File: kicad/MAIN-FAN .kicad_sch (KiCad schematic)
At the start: 8 parts, among them J14 MAIN-FAN, Q14 AO3401, Q15 2N3904

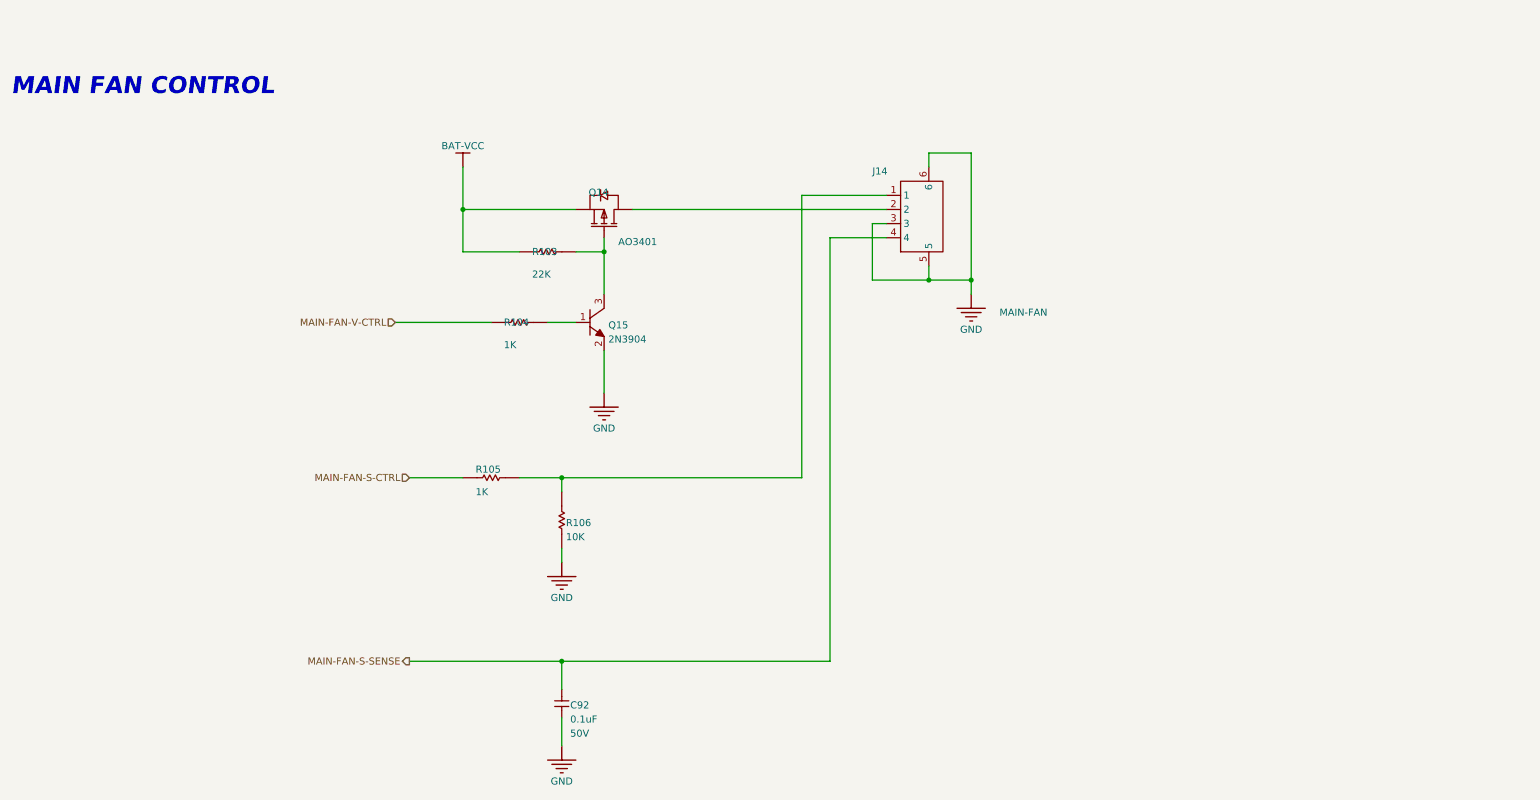
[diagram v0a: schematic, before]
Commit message: Added Pi CM4/CM5
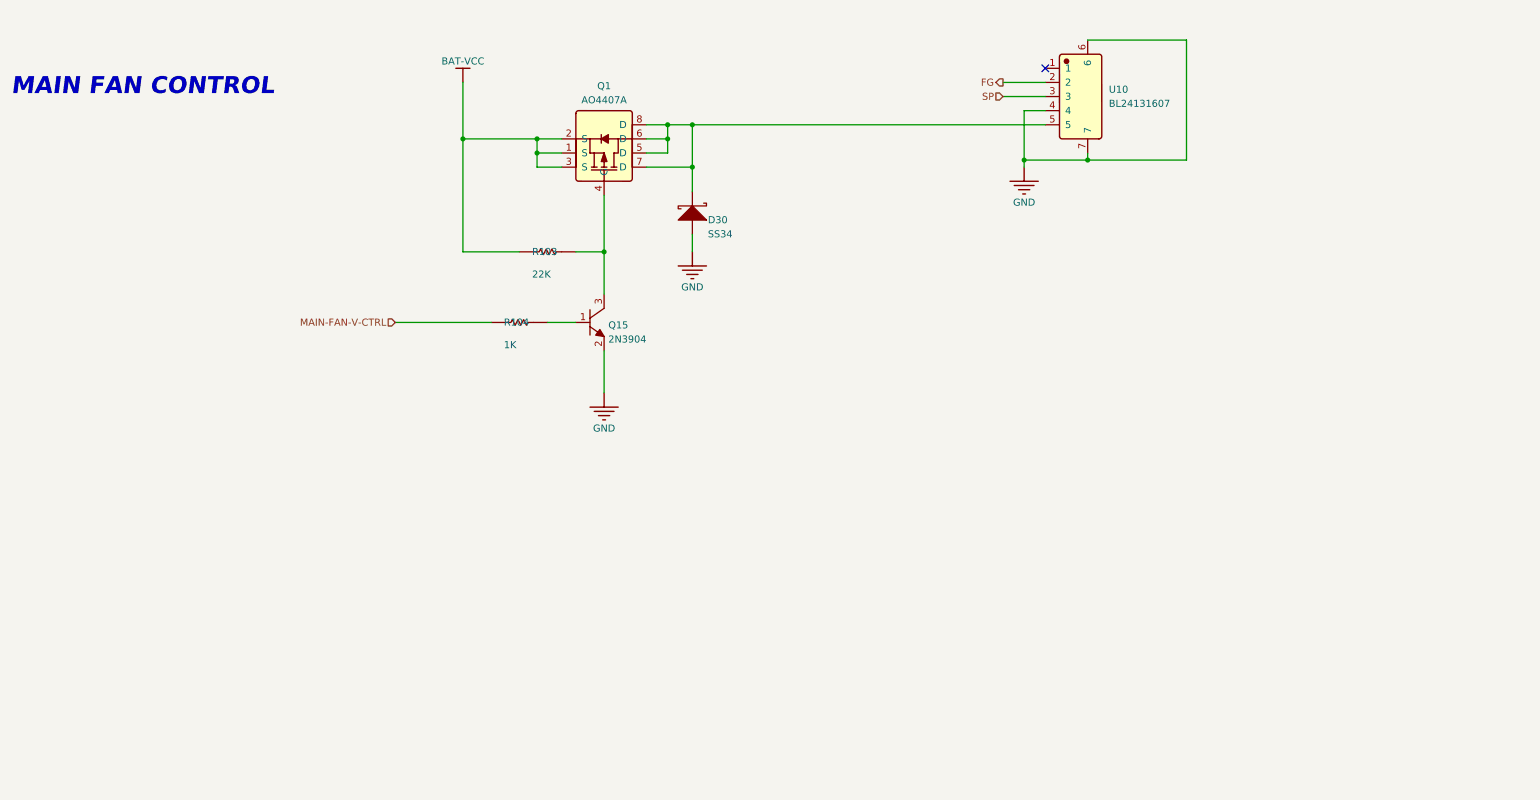
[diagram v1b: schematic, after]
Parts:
- removed C92: 0.1uF, oomwoo_altium:CAP-0402, symbol DesignLibrary:MAIN-FAN_3_Capacitor-1_DesignLibrary.SchLib
- removed J14: MAIN-FAN, oomwoo_altium:CONN-SMD_4P-P2.00_XUNPU_WAFER-PH2.0-4PWB, symbol DesignLibrary:MAIN-FAN_0_HDRx4_DesignLibrary.SchLib
- removed Q14: AO3401, oomwoo_altium:SOT23-3D, symbol DesignLibrary:MAIN-FAN_1_mirrored_P-MOS-SOT23_DesignLibrary.SchLib
- removed R105: 1K, oomwoo_altium:RES-0402, symbol DesignLibrary:MAIN-FAN_2_Resistor-1_DesignLibrary.SchLib
- removed R106: 10K, oomwoo_altium:RES-0402, symbol DesignLibrary:MAIN-FAN_1_Resistor-1_DesignLibrary.SchLib
- added D30: SS34, oomwoo_altium:SMA, symbol DesignLibrary:MAIN-BRUSH MOTOR_1_DIODE-2_DesignLibrary.SchLib
- added Q1: AO4407A, JLCImport:AO4407A, symbol JLCImport:AO4407A
- added U10: BL24131607, JLCImport:S5B-PH-SM4-TB_LF_SN, symbol JLCImport:S5B-PH-SM4-TB_LF_SN
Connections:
- net BAT-VCC: now also Q1.1 (S), Q1.2 (S), Q1.3 (S)
- net GND: now also D30.1 (A), U10.4, U10.6, U10.7
- net at Q15.3 (C), R103.2: now also Q1.4 (G)
- new net: D30.2 (K), Q1.5 (D), Q1.6 (D), Q1.7 (D), Q1.8 (D), U10.5
- new net FG: U10.2
- new net SP: U10.3
- no-connect marks 0 -> 1

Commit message: Changed MCU to STM32G473VCT6
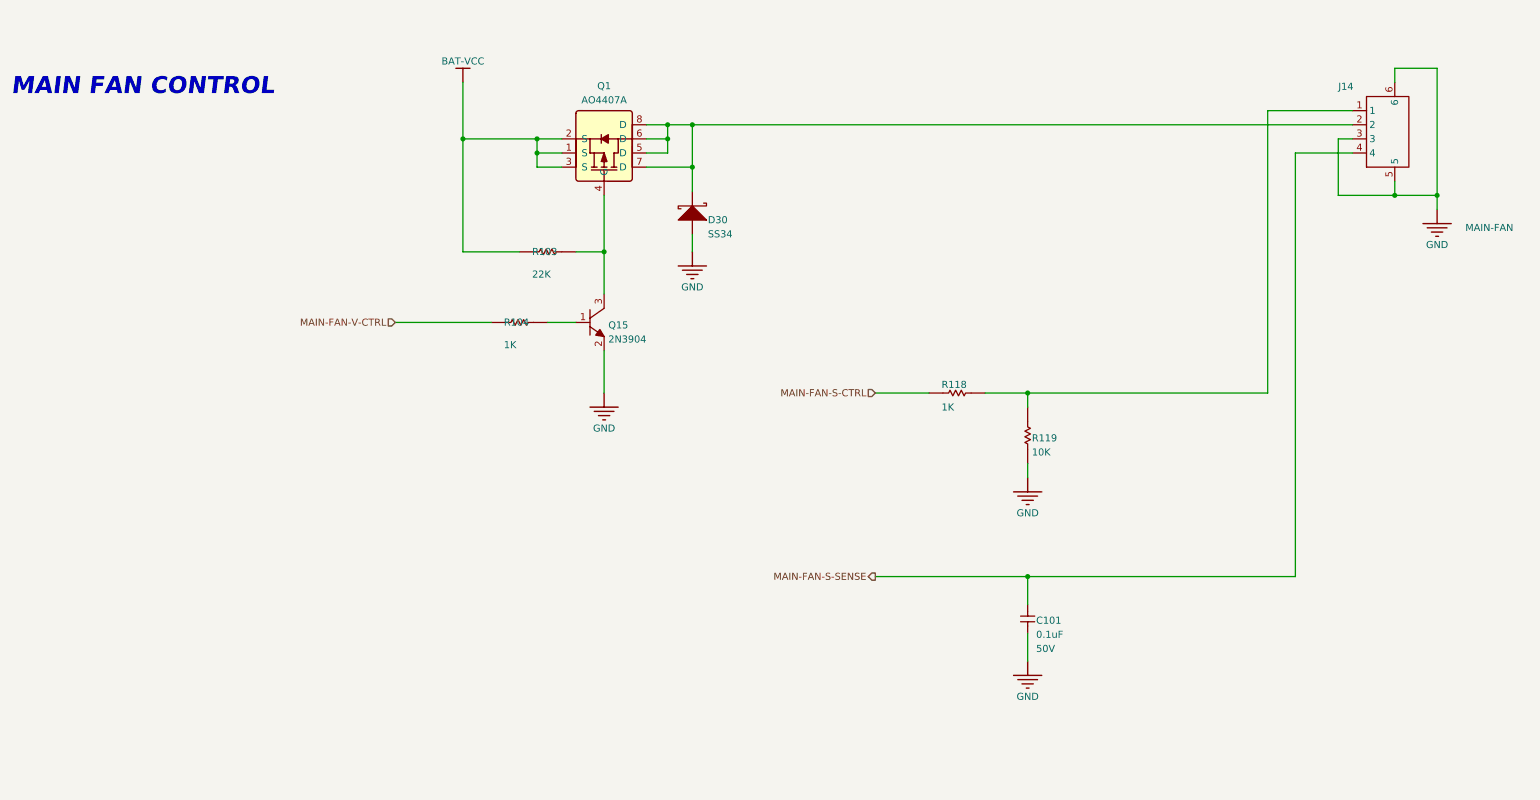
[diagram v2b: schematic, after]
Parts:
- removed U10: BL24131607, JLCImport:S5B-PH-SM4-TB_LF_SN, symbol JLCImport:S5B-PH-SM4-TB_LF_SN
- added C101: 0.1uF, Capacitor_SMD:C_0603_1608Metric, symbol DesignLibrary:MAIN-FAN_3_Capacitor-1_DesignLibrary.SchLib
- added J14: MAIN-FAN, oomwoo_altium:CONN-SMD_4P-P2.00_XUNPU_WAFER-PH2.0-4PWB, symbol DesignLibrary:MAIN-FAN_0_HDRx4_DesignLibrary.SchLib
- added R118: 1K, Resistor_SMD:R_0603_1608Metric, symbol DesignLibrary:MAIN-FAN_2_Resistor-1_DesignLibrary.SchLib
- added R119: 10K, Resistor_SMD:R_0603_1608Metric, symbol DesignLibrary:MAIN-FAN_1_Resistor-1_DesignLibrary.SchLib
- R103, R104: footprint oomwoo_altium:RES-0402 -> Resistor_SMD:R_0603_1608Metric
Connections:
- net GND: now also C101.2, J14.3, J14.5, J14.6, R119.1
- net at D30.2 (K), Q1.5 (D), Q1.6 (D)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: now also J14.2
- new net: J14.1, R118.1, R119.2
- new net MAIN-FAN-S-CTRL: R118.2
- new net MAIN-FAN-S-SENSE: C101.1, J14.4
- no-connect marks 1 -> 0

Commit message: STM32G473VCT6
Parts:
- removed Q15: 2N3904, oomwoo_altium:SOT23-3D, symbol DesignLibrary:MAIN-FAN_0_NPN-SOT23_DesignLibrary.SchLib
- added Q9: IRLML6344TRPBF, JLCImport:IRLML6344TRPBF, symbol JLCImport:IRLML6344TRPBF
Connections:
- net GND: now also Q9.2 (S)
- net at R104.2: now also Q9.1 (G)
- net at Q1.4 (G), R103.2: now also Q9.3 (D)
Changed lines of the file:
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@@
+	(wire
+		(pts
+			(xy 276.225 160.655) (xy 278.765 160.655)
+		)
+		(stroke
+			(width 0)
+			(type default)
+		)
+	)
 	(wire
 		(pts
@@
 		(pts
 			(xy 260.985 127.635) (xy 260.985 147.955)
-		)
-		(stroke
-			(width 0)
-			(type default)
-		)
-	)
-	(wire
-		(pts
-			(xy 276.225 160.655) (xy 281.305 160.655)
 		)
 		(stroke
@@
 			)
 			(justify right)
-		)
-	)
-	(symbol
-		(lib_id "DesignLibrary:MAIN-FAN_0_NPN-SOT23_DesignLibrary.SchLib")
-		(at 281.305 155.575 90)
-		(unit 1)
-		(body_style 1)
-		(exclude_from_sim no)
-		(in_bom yes)
-		(on_board yes)
-		(in_pos_files yes)
-		(dnp no)
-		(property "Reference" "Q15"
-			(at 287.147 160.401 90)
-			(show_name no)
-			(do_not_autoplace no)
-			(effects
-				(font
-					(size 1.27 1.27)
-				)
-				(justify right bottom)
-			)
-		)
-		(property "Value" "2N3904"
-			(at 287.147 162.941 90)
-			(show_name no)
-			(do_not_autoplace no)
-			(effects
-				(font
-					(size 1.27 1.27)
-				)
-				(justify right bottom)
-			)
-		)
-		(property "Footprint" "oomwoo_altium:SOT23-3D"
-			(at 281.305 155.575 0)
-			(hide yes)
-			(show_name no)
-			(do_not_autoplace no)
-			(effects
-				(font
-					(size 1.27 1.27)
-				)
-			)
-		)
-		(property "Datasheet" ""
-			(at 281.305 155.575 0)
-			(hide yes)
-			(show_name no)
-			(do_not_autoplace no)
-			(effects
-				(font
-					(size 1.27 1.27)
-				)
-			)
-		)
-		(property "Description" ""
-			(at 281.305 155.575 0)
-			(hide yes)
-			(show_name no)
-			(do_not_autoplace no)
-			(effects
-				(font
-					(size 1.27 1.27)
-				)
-			)
-		)
-		(property "MANUFACTURINGPARTNUMBER" "*"
-			(at 280.797 155.067 90)
-			(hide yes)
-			(show_name no)
-			(do_not_autoplace no)
-			(effects
-				(font
-					(size 1.27 1.27)
-				)
-				(justify right bottom)
-			)
-		)
-		(property "MANUFACTURER" "*"
-			(at 280.797 155.067 90)
-			(hide yes)
-			(show_name no)
-			(do_not_autoplace no)
-			(effects
-				(font
-					(size 1.27 1.27)
-				)
-				(justify right bottom)
-			)
-		)
-		(property "SUPPLIERPARTNUMBER" "*"
-			(at 280.797 155.067 90)
-			(hide yes)
-			(show_name no)
-			(do_not_autoplace no)
-			(effects
-				(font
-					(size 1.27 1.27)
-				)
-				(justify right bottom)
-			)
-		)
-		(property "SUPPLIER" "*"
-			(at 280.797 155.067 90)
-			(hide yes)
-			(show_name no)
-			(do_not_autoplace no)
-			(effects
-				(font
-					(size 1.27 1.27)
-				)
-				(justify right bottom)
-			)
-		)
-		(property "VOLTAGERATE" "*"
-			(at 280.797 155.067 90)
-			(hide yes)
-			(show_name no)
-			(do_not_autoplace no)
-			(effects
-				(font
-					(size 1.27 1.27)
-				)
-				(justify right bottom)
-			)
-		)
-		(pin "1"
-		)
-		(pin "2"
-		)
-		(pin "3"
-		)
-		(instances
-			(project "oomwoo-kicad"
-				(path "/dbcfb655-8d45-4808-9a74-2a0eb03372e8/43bddca0-8e54-471a-b352-8abb91be7702"
-					(reference "Q15")
-					(unit 1)
-				)
-			)
 		)
 	)
@@
 					(unit 1)
 				)
+			)
+		)
+	)
+	(symbol
+		(lib_id "JLCImport:IRLML6344TRPBF")
+		(at 283.845 160.655 0)
+		(unit 1)
+		(body_style 1)
+		(exclude_from_sim no)
+		(in_bom yes)
+		(on_board yes)
+		(in_pos_files yes)
+		(dnp no)
+		(fields_autoplaced yes)
+		(property "Reference" "Q9"
+			(at 291.465 159.3849 0)
+			(show_name no)
+			(do_not_autoplace no)
+			(effects
+				(font
+					(size 1.27 1.27)
+				)
+				(justify left)
+			)
+		)
+		(property "Value" "IRLML6344TRPBF"
+			(at 291.465 161.9249 0)
+			(show_name no)
+			(do_not_autoplace no)
+			(effects
+				(font
+					(size 1.27 1.27)
+				)
+				(justify left)
+			)
+		)
+		(property "Footprint" "JLCImport:IRLML6344TRPBF"
+			(at 283.845 160.655 0)
+			(hide yes)
+			(show_name no)
+			(do_not_autoplace no)
+			(effects
+				(font
+					(size 1.27 1.27)
+				)
+			)
+		)
+		(property "Datasheet" "https://www.lcsc.com/datasheet/lcsc_datasheet_1809200041_Infineon-Technologies-IRLML6344TRPBF_C53550.pdf"
+			(at 283.845 160.655 0)
+			(hide yes)
+			(show_name no)
+			(do_not_autoplace no)
+			(effects
+				(font
+					(size 1.27 1.27)
+				)
+			)
+		)
+		(property "Description" "-55℃~+150℃ 1 N-channel 1.1V 1.3W 29mΩ@4.5V 30V 46pF 5A 6.8nC 650pF SOT-23 MOSFETs ROHS"
+			(at 283.845 160.655 0)
+			(hide yes)
+			(show_name no)
+			(do_not_autoplace no)
+			(effects
+				(font
+					(size 1.27 1.27)
+				)
+			)
+		)
+		(property "LCSC" "C53550"
+			(at 283.845 160.655 0)
+			(hide yes)
+			(show_name no)
+			(do_not_autoplace no)
+			(effects
+				(font
+					(size 1.27 1.27)
+				)
+			)
+		)
+		(property "Manufacturer" "Infineon Technologies"
+			(at 283.845 160.655 0)
+			(hide yes)
+			(show_name no)
+			(do_not_autoplace no)
+			(effects
+				(font
+					(size 1.27 1.27)
+				)
+			)
+		)
+		(property "Manufacturer Part" "IRLML6344TRPBF"
+			(at 283.845 160.655 0)
+			(hide yes)
+			(show_name no)
+			(do_not_autoplace no)
+			(effects
+				(font
+					(size 1.27 1.27)
+				)
+			)
+		)
+		(pin "2"
+		)
+		(pin "3"
+		)
+		(pin "1"
+		)
+		(instances
+			(project "oomwoo-kicad"
+				(path "/dbcfb655-8d45-4808-9a74-2a0eb03372e8/43bddca0-8e54-471a-b352-8abb91be7702"
+					(reference "Q9")
+					(unit 1)
+				)

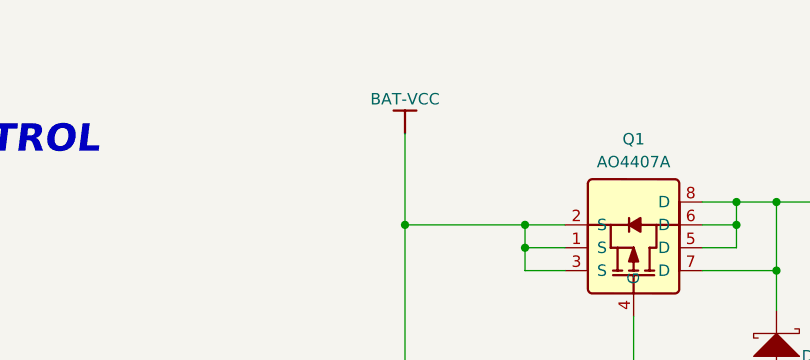
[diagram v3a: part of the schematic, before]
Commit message: RTC clock, signal integrity
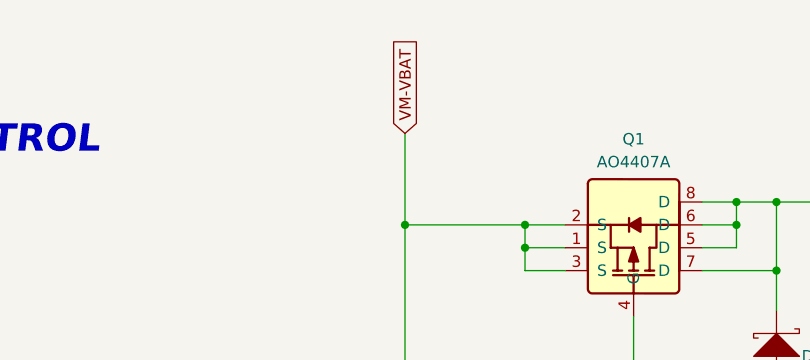
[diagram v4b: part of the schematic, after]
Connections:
- net BAT-VCC renamed VM-VBAT
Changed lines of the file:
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@@
+		)
+	)
+	(global_label "VM-VBAT"
+		(shape input)
+		(at 260.985 117.475 90)
+		(fields_autoplaced yes)
+		(effects
+			(font
+				(size 1.27 1.27)
+			)
+			(justify left)
+		)
+		(property "Intersheetrefs" "${INTERSHEET_REFS}"
+			(at 260.985 105.9626 90)
+			(hide yes)
+			(show_name no)
+			(do_not_autoplace no)
+			(effects
+				(font
+					(size 1.27 1.27)
+				)
+				(justify left)
+			)
 		)
 	)
@@
 					(unit 1)
 				)
-			)
-		)
-	)
-	(symbol
-		(lib_id "oomwoo-kicad-altium-import:BAT-VCC_BAR")
-		(at 260.985 117.475 180)
-		(unit 1)
-		(body_style 1)
-		(exclude_from_sim no)
-		(in_bom yes)
-		(on_board yes)
-		(in_pos_files yes)
-		(dnp no)
-		(property "Reference" "#PWR0585"
-			(at 260.985 117.475 0)
-			(hide yes)
-			(show_name no)
-			(do_not_autoplace no)
-			(effects
-				(font
-					(size 1.27 1.27)
-				)
-			)
-		)
-		(property "Value" "BAT-VCC"
-			(at 260.985 113.665 0)
-			(show_name no)
-			(do_not_autoplace no)
-			(effects
-				(font
-					(size 1.27 1.27)
-				)
-			)
-		)
-		(property "Footprint" ""
-			(at 260.985 117.475 0)
-			(show_name no)
-			(do_not_autoplace no)
-			(effects
-				(font
-					(size 1.27 1.27)
-				)
-			)
-		)
-		(property "Datasheet" ""
-			(at 260.985 117.475 0)
-			(show_name no)
-			(do_not_autoplace no)
-			(effects
-				(font
-					(size 1.27 1.27)
-				)
-			)
-		)
-		(property "Description" ""
-			(at 260.985 117.475 0)
-			(show_name no)
-			(do_not_autoplace no)
-			(effects
-				(font
-					(size 1.27 1.27)
-				)
-			)
-		)
-		(pin ""
-		)
-		(instances
-			(project "oomwoo-kicad"
-				(path "/dbcfb655-8d45-4808-9a74-2a0eb03372e8/43bddca0-8e54-471a-b352-8abb91be7702"
-					(reference "#PWR0585")
-					(unit 1)
-				)
